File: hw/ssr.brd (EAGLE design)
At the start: 136.2 x 222.2 mm, 86 parts, among them T1 BC328, T2 BC328, T3 BC328, T4 BC328, T5 BC328

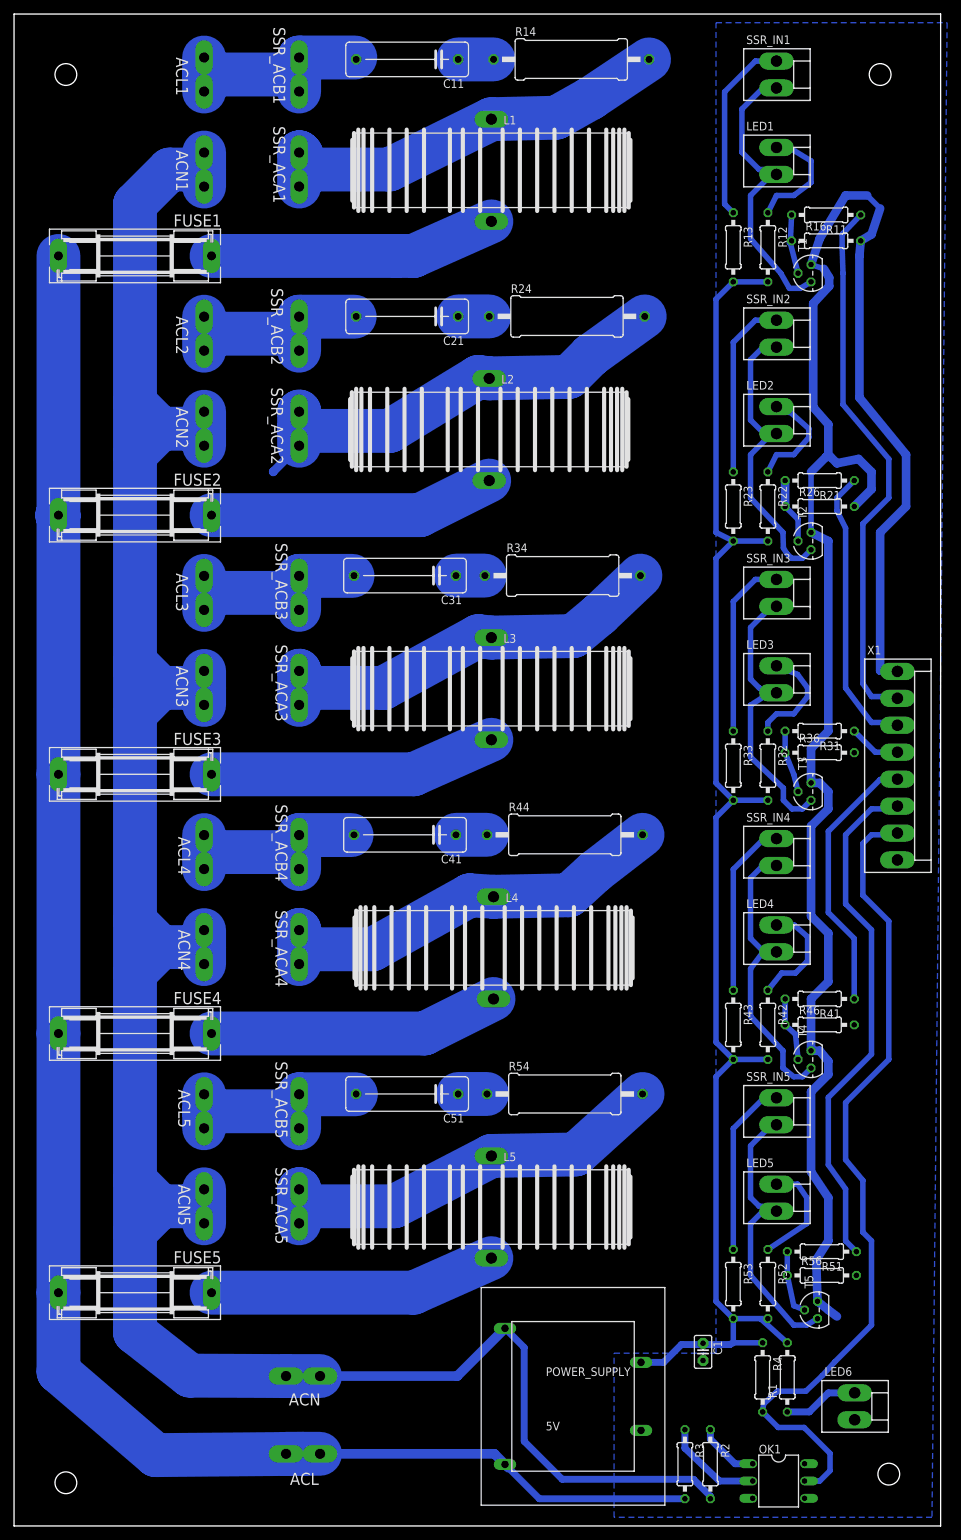
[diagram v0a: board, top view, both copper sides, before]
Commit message: Adapt schematic and board layout according to new parts.
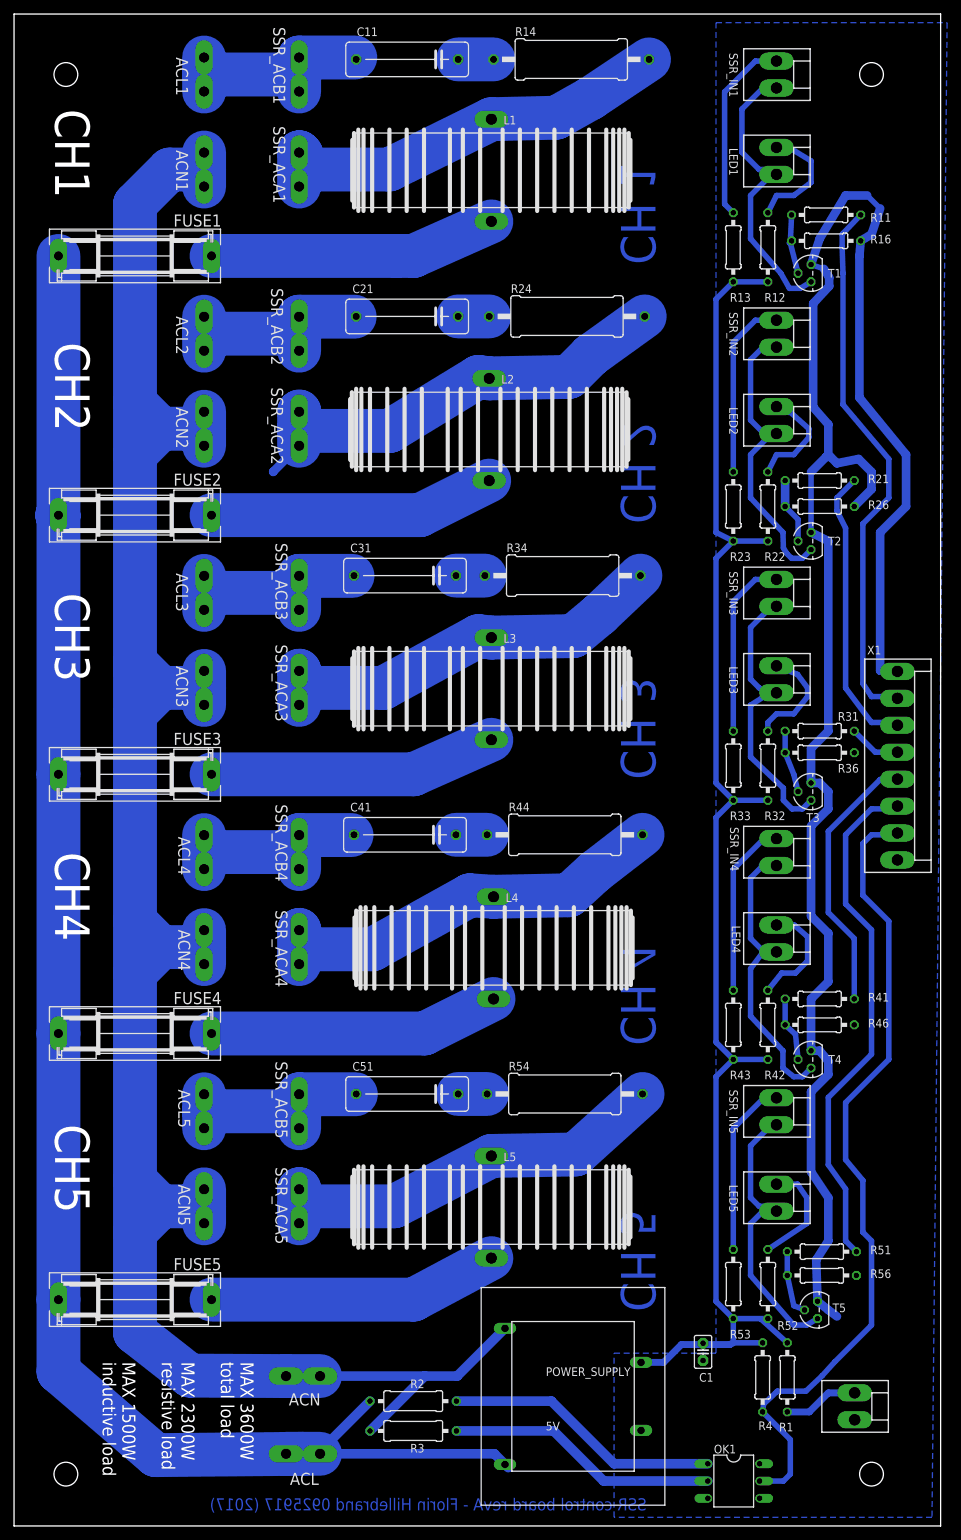
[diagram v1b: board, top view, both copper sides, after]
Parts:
- LED1: value (none) -> LED1
- LED2: value (none) -> LED2
- LED3: value (none) -> LED3
- LED4: value (none) -> LED4
- LED5: value (none) -> LED5
- LED6: value (none) -> POWER LED
- R1: value (none) -> 270R
- R16, R26, R36, R46, R56: value (none) -> 0R
- R2, R3: device parts:0207/10 -> resistor:0309/12
- R4: value (none) -> 56K
- SSR_IN1: value (none) -> SSR1
- SSR_IN2: value (none) -> SSR2
- SSR_IN3: value (none) -> SSR3
- SSR_IN4: value (none) -> SSR4
- SSR_IN5: value (none) -> SSR5
- X1: value (none) -> uC
- moved R2 44.7 mm to (-80.1, -92.1), turned to 180 degrees
- moved R3 40.2 mm to (-80.1, -96.5), turned to 180 degrees
- moved OK1 6.60 mm to (-33.0, -103.9)
- moved FUSE5 1.02 mm to (-121.0, -77.2)
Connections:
- net ACL: now also R2.2; no longer R3.2
- net ACN: now also R3.2; no longer R2.2
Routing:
- net ACN: track 383.6 -> 346.1 mm
- net N$7: track 9.12 -> 40.8 mm
- net N$6: track 14.6 -> 40.0 mm
- net ACL: track 266.8 -> 249.0 mm
- net ZC: track 123.3 -> 119.7 mm
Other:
- board text added: "CH 1"
- board text added: "CH 2"
- board text added: "CH 3"
- board text added: "CH 4"
- board text added: "CH 5"
- board text added: "CH1"
- board text added: "CH2"
- board text added: "CH3"
- board text added: "CH4"
- board text added: "CH5"
- board text added: "MAX 3600W total load MAX 2300W resistive load MAX 1500W inductive load"
- board text added: "SSR control board revA - Florin Hillebrand 0925917 (2017)"

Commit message: hw: update PCB layout and outputs.
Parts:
- added DRILEGEND: (no value), drilegend:DRILEGEND
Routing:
- net SSR_ACA2: track 66.8 -> 61.4 mm
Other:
- board text added: "01-16"
- board text added: "01-20"
- board text added: "LAYER-STACK"
